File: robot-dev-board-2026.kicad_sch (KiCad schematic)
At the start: 0 parts

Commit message: added stuff
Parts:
- added U1: RP2040, Package_DFN_QFN:QFN-56-1EP_7x7mm_P0.4mm_EP3.2x3.2mm, symbol MCU_RaspberryPi:RP2040
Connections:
- new net: U1.1 (IOVDD), U1.10 (IOVDD), U1.22 (IOVDD), U1.33 (IOVDD), U1.42 (IOVDD), U1.49 (IOVDD)
- new net: U1.23 (DVDD), U1.50 (DVDD)
- new net GND: U1.57 (GND)
- new net GPIO0: U1.2 (GPIO0)
- new net GPIO1: U1.3 (GPIO1)
- new net GPIO10: U1.13 (GPIO10)
- new net GPIO11: U1.14 (GPIO11)
- new net GPIO12: U1.15 (GPIO12)
- new net GPIO13: U1.16 (GPIO13)
- new net GPIO14: U1.17 (GPIO14)
- new net GPIO15: U1.18 (GPIO15)
- new net GPIO16: U1.27 (GPIO16)
- new net GPIO17: U1.28 (GPIO17)
- new net GPIO18: U1.29 (GPIO18)
- new net GPIO19: U1.30 (GPIO19)
- new net GPIO2: U1.4 (GPIO2)
- new net GPIO20: U1.31 (GPIO20)
- new net GPIO21: U1.32 (GPIO21)
- new net GPIO22: U1.34 (GPIO22)
- new net GPIO23: U1.35 (GPIO23)
- new net GPIO24: U1.36 (GPIO24)
- new net GPIO25: U1.37 (GPIO25)
- new net GPIO26: U1.38 (GPIO26_ADC0)
- new net GPIO27: U1.39 (GPIO27_ADC1)
- new net GPIO28: U1.40 (GPIO28_ADC2)
- new net GPIO29: U1.41 (GPIO29_ADC3)
- new net GPIO3: U1.5 (GPIO3)
- new net GPIO4: U1.6 (GPIO4)
- new net GPIO5: U1.7 (GPIO5)
- new net GPIO6: U1.8 (GPIO6)
- new net GPIO7: U1.9 (GPIO7)
- new net GPIO8: U1.11 (GPIO8)
- new net GPIO9: U1.12 (GPIO9)
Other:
- title: (none) -> Robot Development Board

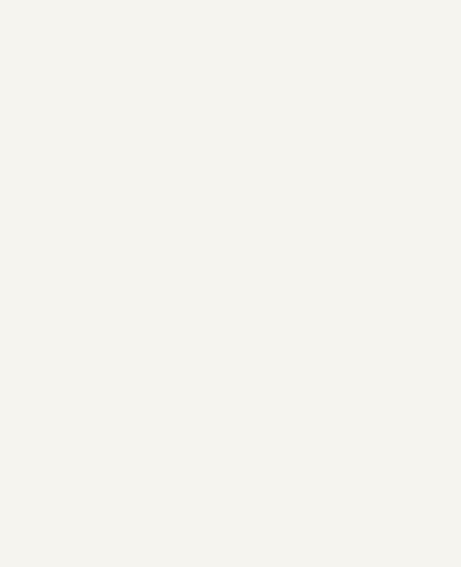
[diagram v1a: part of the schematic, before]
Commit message: added led 2
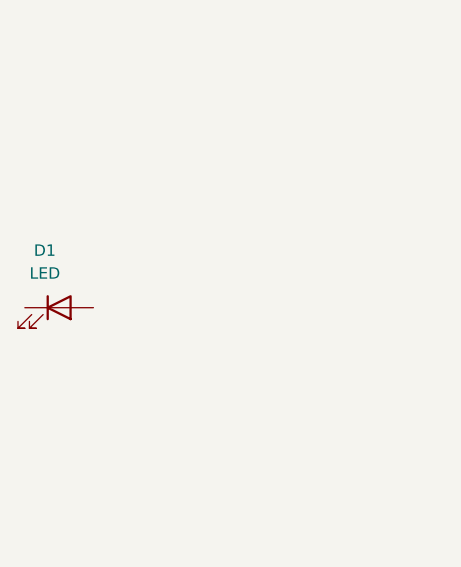
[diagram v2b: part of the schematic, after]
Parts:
- added D1: LED, symbol Device:LED
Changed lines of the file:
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@@
+	)
+	(symbol
+		(lib_id "Device:LED")
+		(at 107.95 102.87 0)
+		(unit 1)
+		(exclude_from_sim no)
+		(in_bom yes)
+		(on_board yes)
+		(dnp no)
+		(fields_autoplaced yes)
+		(property "Reference" "D1"
+			(at 106.3625 96.52 0)
+			(effects
+				(font
+					(size 1.27 1.27)
+				)
+			)
+		)
+		(property "Value" "LED"
+			(at 106.3625 99.06 0)
+			(effects
+				(font
+					(size 1.27 1.27)
+				)
+			)
+		)
+		(property "Footprint" ""
+			(at 107.95 102.87 0)
+			(effects
+				(font
+					(size 1.27 1.27)
+				)
+				(hide yes)
+			)
+		)
+		(property "Datasheet" "~"
+			(at 107.95 102.87 0)
+			(effects
+				(font
+					(size 1.27 1.27)
+				)
+				(hide yes)
+			)
+		)
+		(property "Description" "Light emitting diode"
+			(at 107.95 102.87 0)
+			(effects
+				(font
+					(size 1.27 1.27)
+				)
+				(hide yes)
+			)
+		)
+		(property "Sim.Pins" "1=K 2=A"
+			(at 107.95 102.87 0)
+			(effects
+				(font
+					(size 1.27 1.27)
+				)
+				(hide yes)
+			)
+		)
+		(pin "1"
+		)
+		(pin "2"
+		)
+		(instances
+			(project ""
+				(path "/bf523f8d-75d7-479b-b431-b3dab10d93ee"
+					(reference "D1")
+					(unit 1)
+				)
+			)
+		)
 	)
 	(symbol

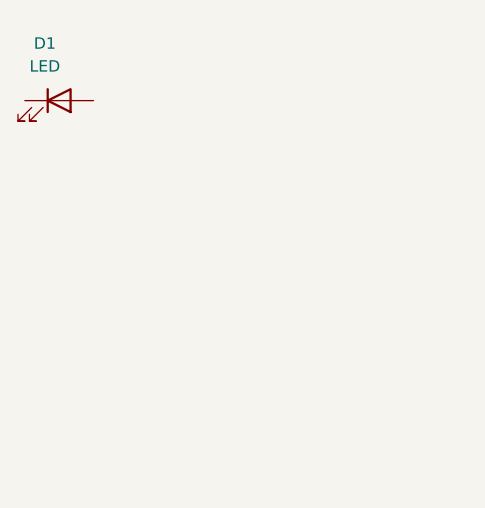
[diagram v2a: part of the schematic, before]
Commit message: adding test resistor
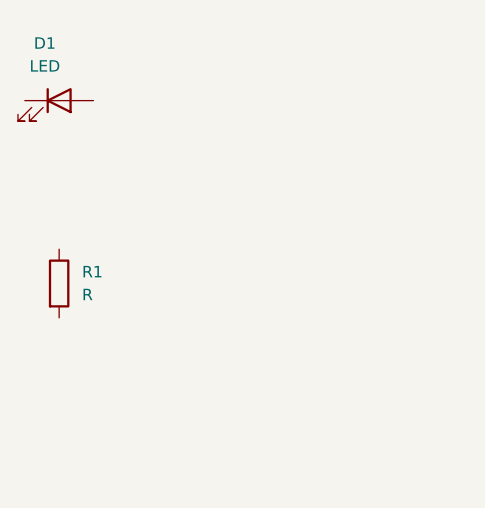
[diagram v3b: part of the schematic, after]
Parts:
- added R1: R, symbol Device:R
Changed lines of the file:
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@@
+	)
+	(symbol
+		(lib_id "Device:R")
+		(at 107.95 123.19 0)
+		(unit 1)
+		(exclude_from_sim no)
+		(in_bom yes)
+		(on_board yes)
+		(dnp no)
+		(fields_autoplaced yes)
+		(property "Reference" "R1"
+			(at 110.49 121.9199 0)
+			(effects
+				(font
+					(size 1.27 1.27)
+				)
+				(justify left)
+			)
+		)
+		(property "Value" "R"
+			(at 110.49 124.4599 0)
+			(effects
+				(font
+					(size 1.27 1.27)
+				)
+				(justify left)
+			)
+		)
+		(property "Footprint" ""
+			(at 106.172 123.19 90)
+			(effects
+				(font
+					(size 1.27 1.27)
+				)
+				(hide yes)
+			)
+		)
+		(property "Datasheet" "~"
+			(at 107.95 123.19 0)
+			(effects
+				(font
+					(size 1.27 1.27)
+				)
+				(hide yes)
+			)
+		)
+		(property "Description" "Resistor"
+			(at 107.95 123.19 0)
+			(effects
+				(font
+					(size 1.27 1.27)
+				)
+				(hide yes)
+			)
+		)
+		(pin "1"
+		)
+		(pin "2"
+		)
+		(instances
+			(project ""
+				(path "/bf523f8d-75d7-479b-b431-b3dab10d93ee"
+					(reference "R1")
+					(unit 1)
+				)
+			)
+		)
 	)
 	(symbol

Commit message: added test component
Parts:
- added U2: MIC4426, symbol Driver_FET:MIC4426
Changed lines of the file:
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@@
+		)
+	)
+	(symbol
+		(lib_id "Driver_FET:MIC4426")
+		(at 69.85 72.39 0)
+		(unit 1)
+		(exclude_from_sim no)
+		(in_bom yes)
+		(on_board yes)
+		(dnp no)
+		(fields_autoplaced yes)
+		(property "Reference" "U2"
+			(at 71.9933 59.69 0)
+			(effects
+				(font
+					(size 1.27 1.27)
+				)
+				(justify left)
+			)
+		)
+		(property "Value" "MIC4426"
+			(at 71.9933 62.23 0)
+			(effects
+				(font
+					(size 1.27 1.27)
+				)
+				(justify left)
+			)
+		)
+		(property "Footprint" ""
+			(at 69.85 80.01 0)
+			(effects
+				(font
+					(size 1.27 1.27)
+				)
+				(hide yes)
+			)
+		)
+		(property "Datasheet" "https://ww1.microchip.com/downloads/en/DeviceDoc/MIC4426-7-8-Dual-1-5A-Peak-Low-Side-MOSFET-DRivers-DS20006202A.pdf"
+			(at 69.85 89.154 0)
+			(effects
+				(font
+					(size 1.27 1.27)
+				)
+				(hide yes)
+			)
+		)
+		(property "Description" "Dual 1.5A-Peak Low-Side MOSFET Driver, 4.5..18V supply voltage, TTL/CMOS compatible inputs, inverting drivers, DIP-8 / SOIC-8 / MSOP-8"
+			(at 69.85 86.614 0)
+			(effects
+				(font
+					(size 1.27 1.27)
+				)
+				(hide yes)
+			)
+		)
+		(pin "7"
+		)
+		(pin "4"
+		)
+		(pin "2"
+		)
+		(pin "3"
+		)
+		(pin "1"
+		)
+		(pin "8"
+		)
+		(pin "5"
+		)
+		(pin "6"
+		)
+		(instances
+			(project ""
+				(path "/bf523f8d-75d7-479b-b431-b3dab10d93ee"
+					(reference "U2")
+					(unit 1)
+				)
+			)
 		)
 	)

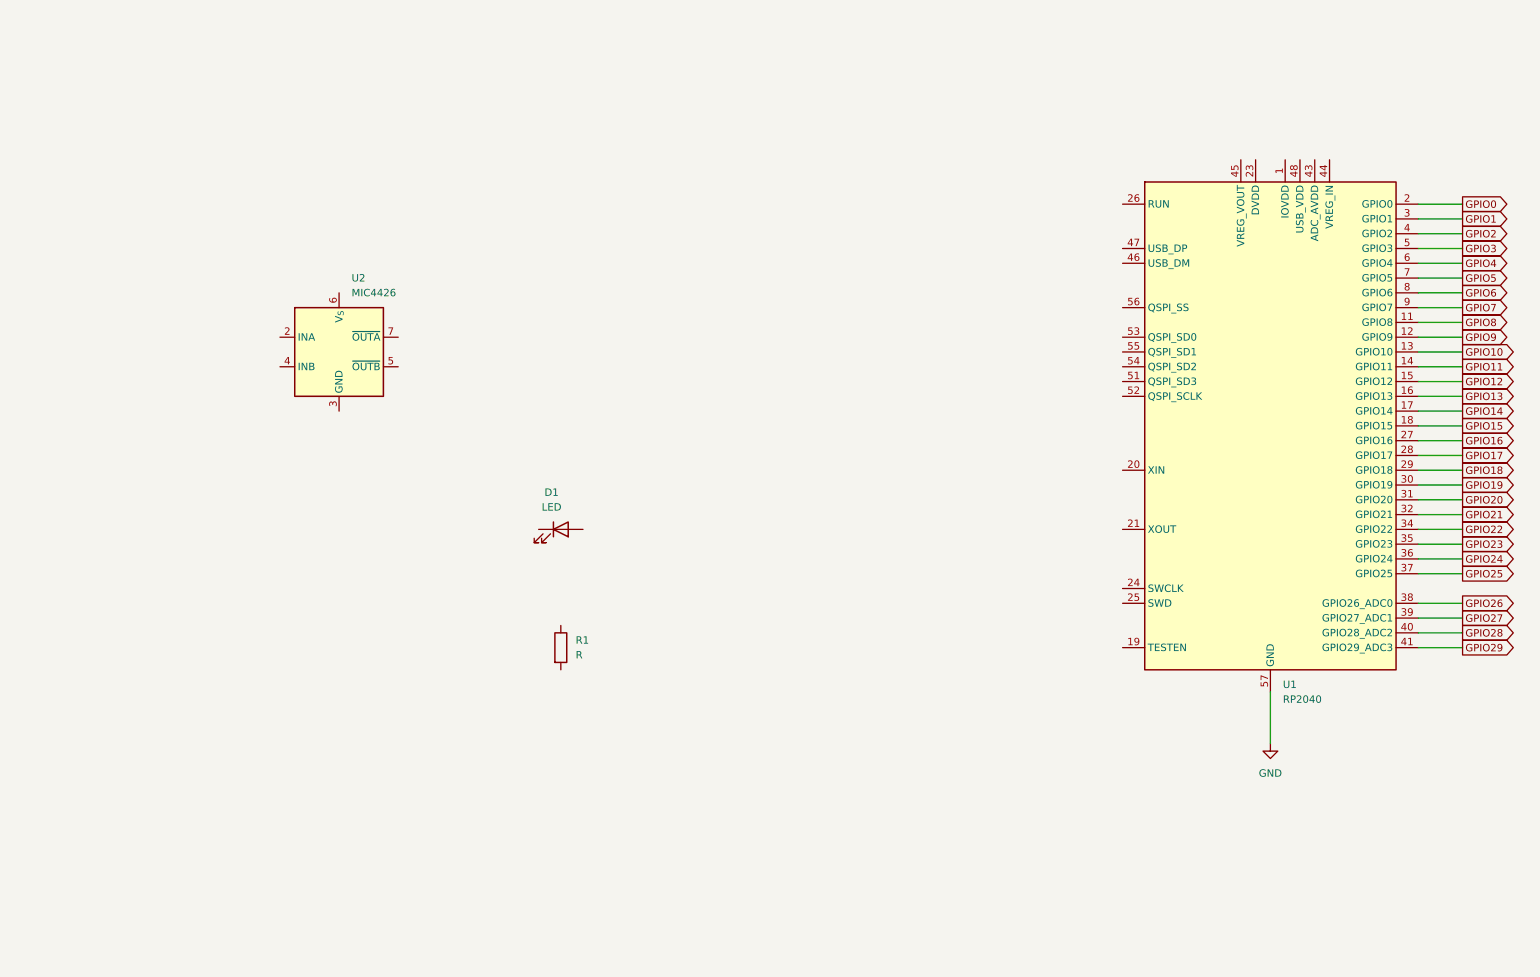
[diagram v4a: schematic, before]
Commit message: updated names for 3v3 labels
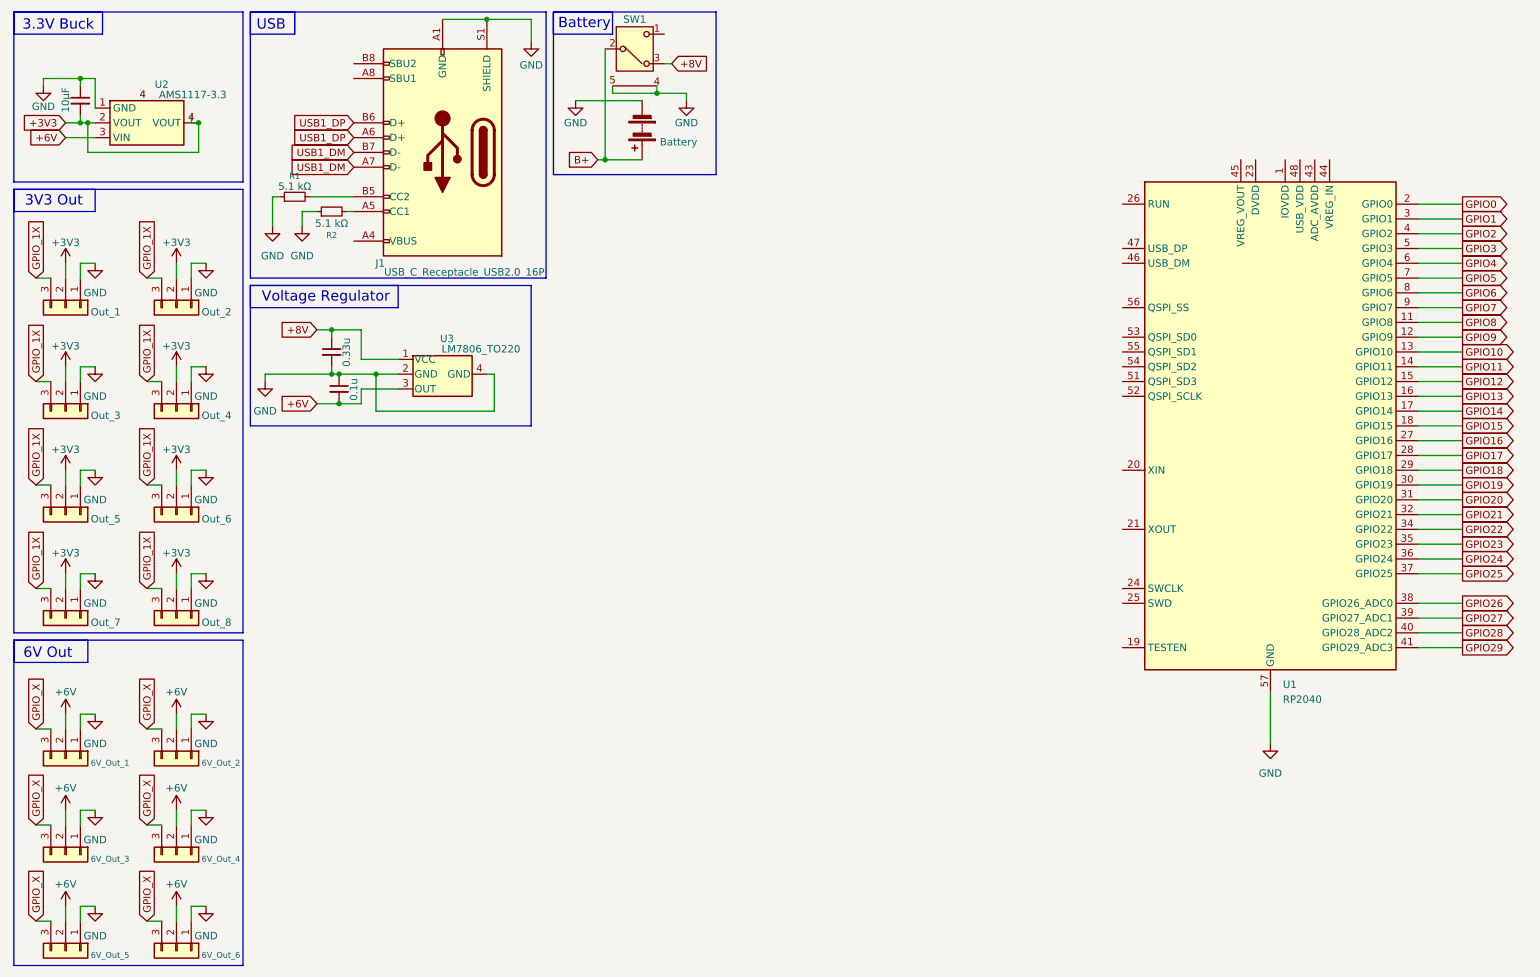
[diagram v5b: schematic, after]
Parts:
- removed D1: LED, symbol Device:LED
- removed R1: R, symbol Device:R
- removed U2: MIC4426, symbol Driver_FET:MIC4426
- added 0.1u, 0.33u, 10µF: C_Small, symbol Device:C_Small
- added BT1: Battery, symbol Device:Battery
- added J1: USB_C_Receptacle_USB2.0_16P, Connector_USB:USB_C_Receptacle_HRO_TYPE-C-31-M-12, symbol Connector:USB_C_Receptacle_USB2.0_16P
- added J10: 6V_Out_1, symbol Connector_Generic:Conn_01x03
- added J11: 6V_Out_2, symbol Connector_Generic:Conn_01x03
- added J12: 6V_Out_3, symbol Connector_Generic:Conn_01x03
- added J13: 6V_Out_4, symbol Connector_Generic:Conn_01x03
- added J14: 6V_Out_5, symbol Connector_Generic:Conn_01x03
- added J15: 6V_Out_6, symbol Connector_Generic:Conn_01x03
- added J2: Out_1, symbol Connector_Generic:Conn_01x03
- added J3: Out_2, symbol Connector_Generic:Conn_01x03
- added J4: Out_3, symbol Connector_Generic:Conn_01x03
- added J5: Out_4, symbol Connector_Generic:Conn_01x03
- added J6: Out_5, symbol Connector_Generic:Conn_01x03
- added J7: Out_6, symbol Connector_Generic:Conn_01x03
- added J8: Out_7, symbol Connector_Generic:Conn_01x03
- added J9: Out_8, symbol Connector_Generic:Conn_01x03
- added R1, R2: 5.1 kΩ, Package_TO_SOT_SMD:Infineon_PG-HDSOP-10-1, symbol Device:R_Small
- added SW1: SW_Nidec_CAS-120A1, Button_Switch_SMD:Nidec_Copal_CAS-120A, symbol Switch:SW_Nidec_CAS-120A1
- added U2: AMS1117-3.3, Package_TO_SOT_SMD:SOT-223-3_TabPin2, symbol Regulator_Linear:AMS1117-3.3
- added U3: LM7806_TO220, Package_TO_SOT_THT:TO-220-3_Vertical, symbol Regulator_Linear:LM7806_TO220
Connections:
- net GND: now also 0.1u.1, 0.33u.2, 10µF.1, BT1.2 (-), J1.A1 (GND), J1.A12 (GND), J1.B1 (GND), J1.B12 (GND), J1.S1 (SHIELD), J10.1 (Pin_1), J11.1 (Pin_1), J12.1 (Pin_1), J13.1 (Pin_1), J14.1 (Pin_1), J15.1 (Pin_1), J2.1 (Pin_1), J3.1 (Pin_1), J4.1 (Pin_1), J5.1 (Pin_1), J6.1 (Pin_1), J7.1 (Pin_1), J8.1 (Pin_1), J9.1 (Pin_1), R1.1, R2.1, U2.1 (GND), U3.2 (GND), U3.4 (GND)
- new net: J1.B5 (CC2), R1.2
- new net: J1.A5 (CC1), R2.2
- new net: J1.A4 (VBUS), J1.A9 (VBUS), J1.B4 (VBUS), J1.B9 (VBUS)
- new net +3V3: 10µF.2, J2.2 (Pin_2), J3.2 (Pin_2), J4.2 (Pin_2), J5.2 (Pin_2), J6.2 (Pin_2), J7.2 (Pin_2), J8.2 (Pin_2), J9.2 (Pin_2), U2.2 (VOUT), U2.4 (VOUT)
- new net +6V: 0.1u.2, J10.2 (Pin_2), J11.2 (Pin_2), J12.2 (Pin_2), J13.2 (Pin_2), J14.2 (Pin_2), J15.2 (Pin_2), U2.3 (VIN), U3.3 (OUT)
- new net +8V: 0.33u.1, SW1.3 (A), U3.1 (VCC)
- new net B+: BT1.1 (+), SW1.2 (B)
- new net GPIO_1X: J2.3 (Pin_3), J3.3 (Pin_3), J4.3 (Pin_3), J5.3 (Pin_3), J6.3 (Pin_3), J7.3 (Pin_3), J8.3 (Pin_3), J9.3 (Pin_3)
- new net GPIO_X: J10.3 (Pin_3), J11.3 (Pin_3), J12.3 (Pin_3), J13.3 (Pin_3), J14.3 (Pin_3), J15.3 (Pin_3)
- new net USB1_DM: J1.A7 (D-), J1.B7 (D-)
- new net USB1_DP: J1.A6 (D+), J1.B6 (D+)
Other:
- note added: "3.3V Buck"
- note added: "3V3 Out"
- note added: "6V Out"
- note added: "Battery"
- note added: "USB"
- note added: "Voltage Regulator"
